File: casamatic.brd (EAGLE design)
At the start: 72.9 x 52.1 mm, 31 parts, among them M1 WIRELESS-NRF24L01SMD, U1 ATTINY85-20PU, U2 AMS1117-3.3, X1 ESP-12

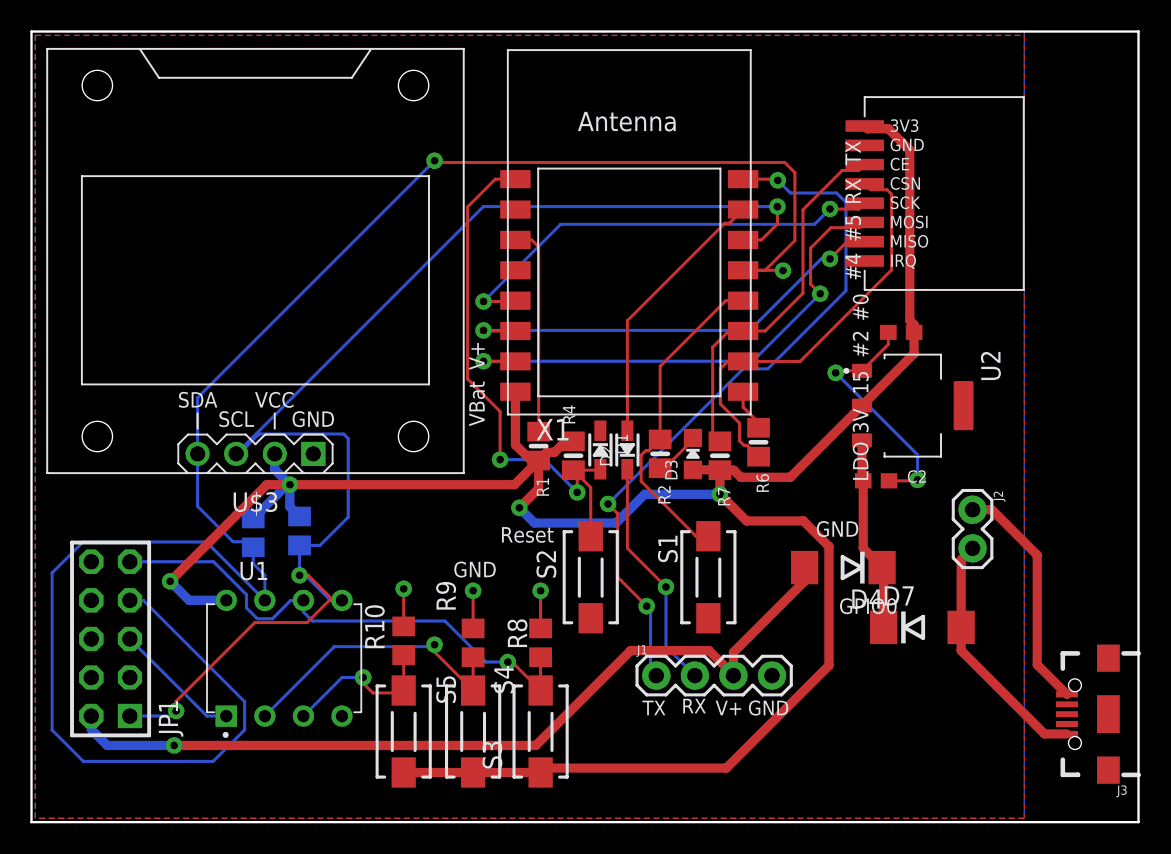
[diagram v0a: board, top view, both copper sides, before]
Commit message: Adjusted design rules - increased drill size by 0.05mm
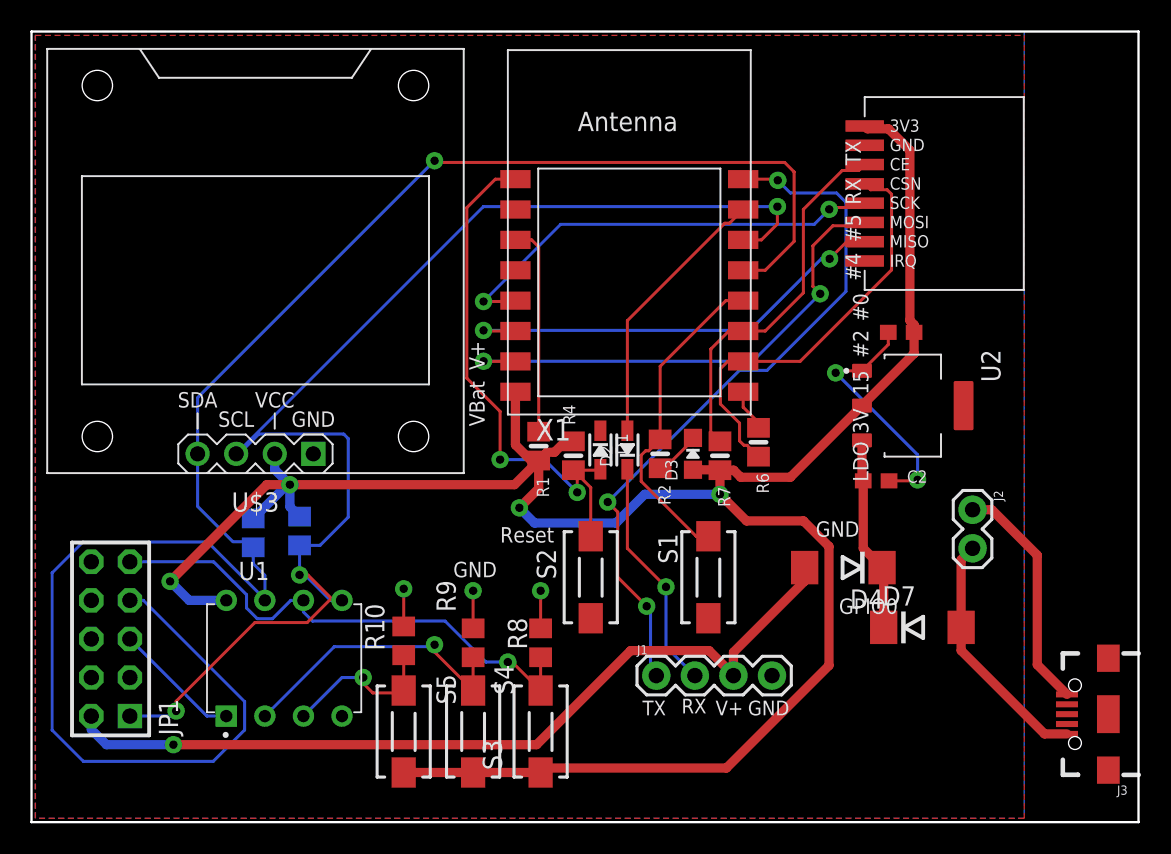
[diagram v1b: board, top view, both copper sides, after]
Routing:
- net GPIO4: track 126.7 -> 124.0 mm, vias 2 -> 1
